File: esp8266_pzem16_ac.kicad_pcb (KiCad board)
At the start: 2 copper layers, 26 x 24 mm, 15 parts, among them J1 RS485, J2 PWR, J3 LED, U1 ESP-12F, U2 AMS1117-3.3

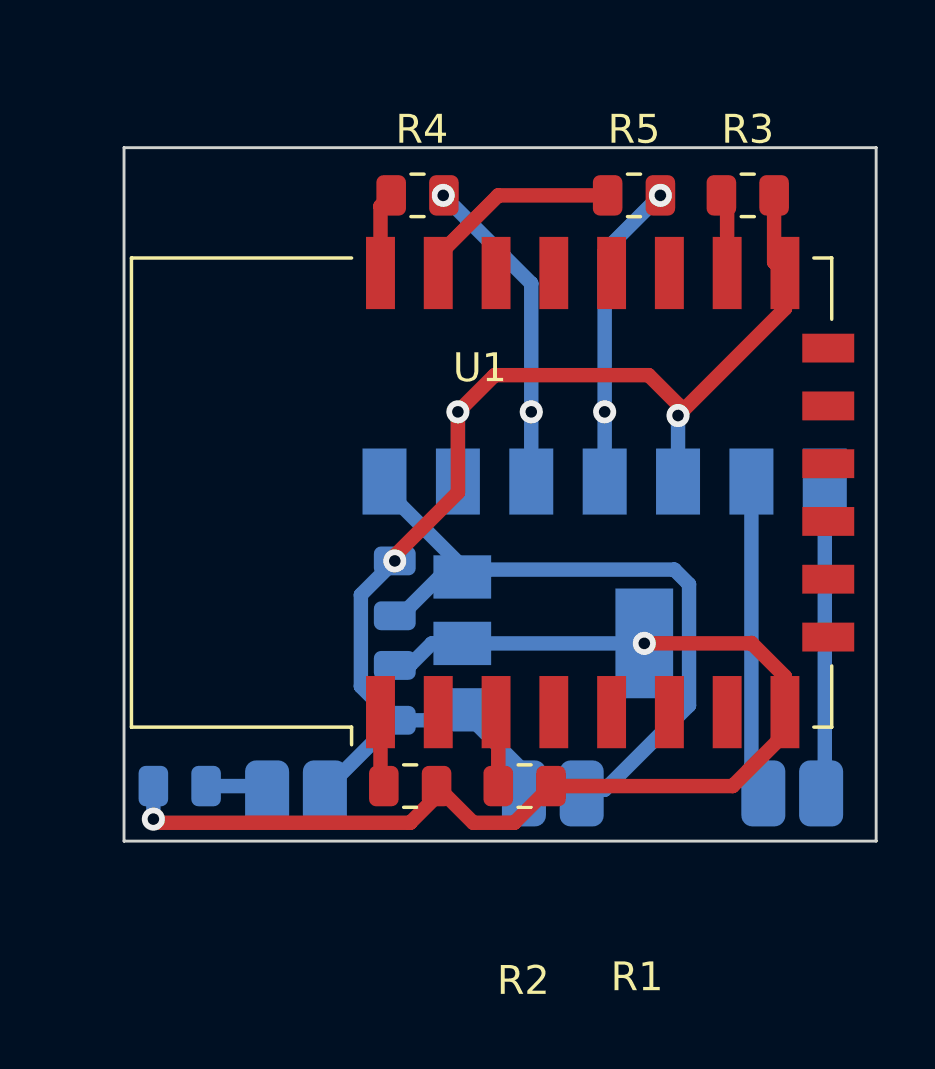
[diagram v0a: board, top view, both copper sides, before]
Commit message: added through hole led pads
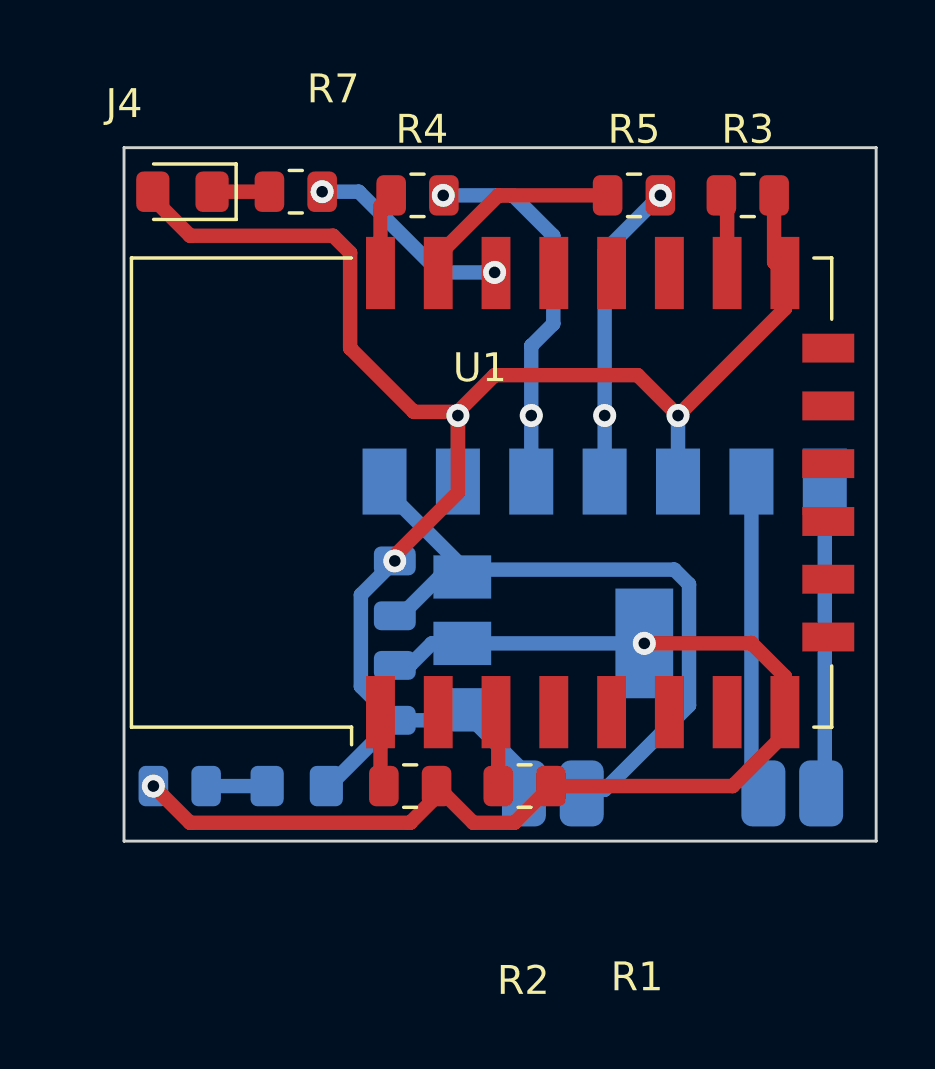
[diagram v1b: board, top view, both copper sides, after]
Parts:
- added J4: LED, LED_SMD:LED_0805_2012Metric_Pad1.15x1.40mm_HandSolder, F.Cu at (62.2, 33.0)
- added R7: 330, Resistor_SMD:R_0805_2012Metric, F.Cu at (66.1, 33.0)
- J3: footprint -local:2pin_pad -> LED_SMD:LED_0805_2012Metric_Pad1.15x1.40mm_HandSolder
- R6: value 0 -> 330
- moved J3 1.06 mm to (66.2, 53.6), turned to 0 degrees
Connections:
- CU1 pad 5: GND -> unconnected-(CU1-Pad5)
- U1 pad 20: unconnected-(U1-Pad20) -> /GPIO_5
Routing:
- net GND: track 44.8 -> 60.3 mm
- net /GPIO_5: track 0.00 -> 7.13 mm, vias 0 -> 2
- net Net-(CU1-Pad3): track 11.2 -> 13.2 mm
- net Net-(J4-Pad1): track 0.00 -> 1.98 mm
- net +3.3V: track 41.9 -> 41.2 mm

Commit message: removed extra files
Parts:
- J3, J4: footprint LED_SMD:LED_0805_2012Metric_Pad1.15x1.40mm_HandSolder -> -local:my_LED_0805_2012Metric_Pad1.15x1.40mm_HandSolder
- moved G*** 1.91 mm to (64.0, 37.0)
- moved R3 0.17 mm to (81.8, 33.0)
- moved R4 0.17 mm to (70.4, 33.0)
- moved R5 0.17 mm to (77.9, 33.0)

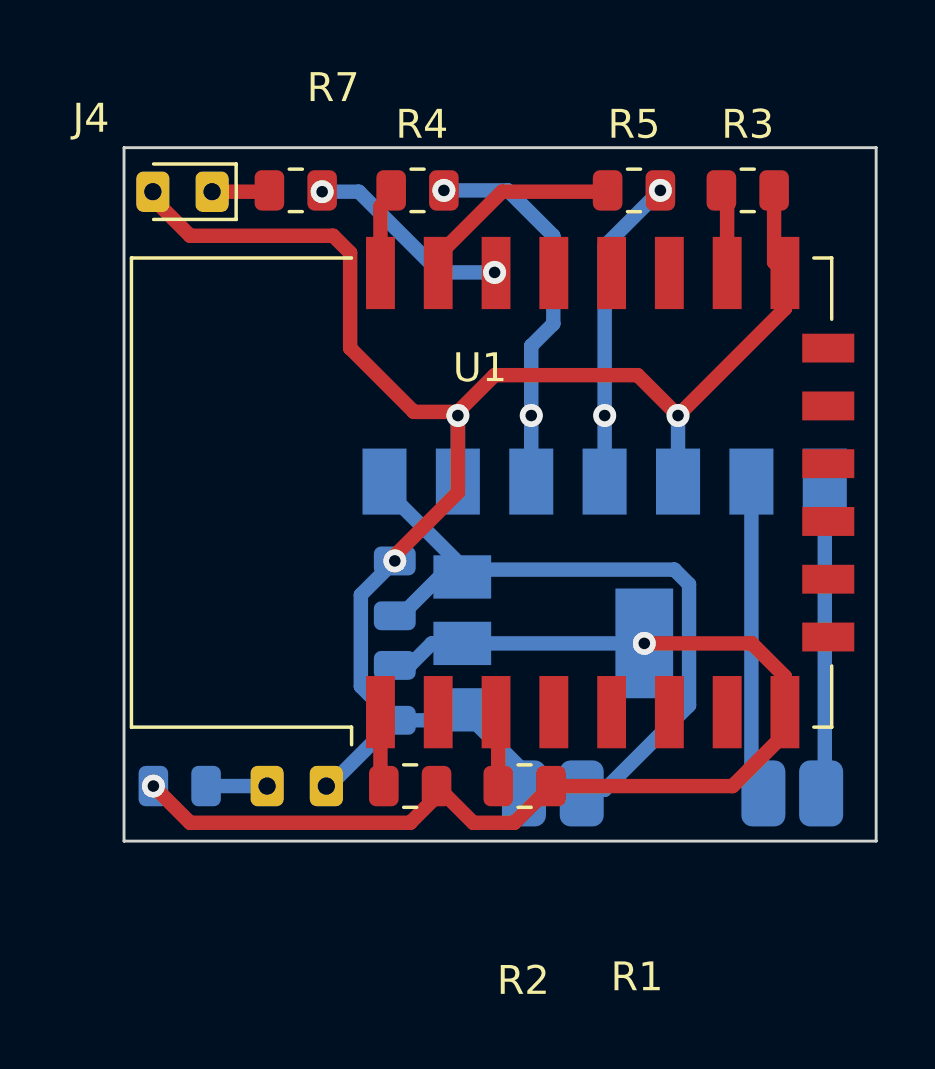
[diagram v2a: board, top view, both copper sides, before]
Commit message: removed more files
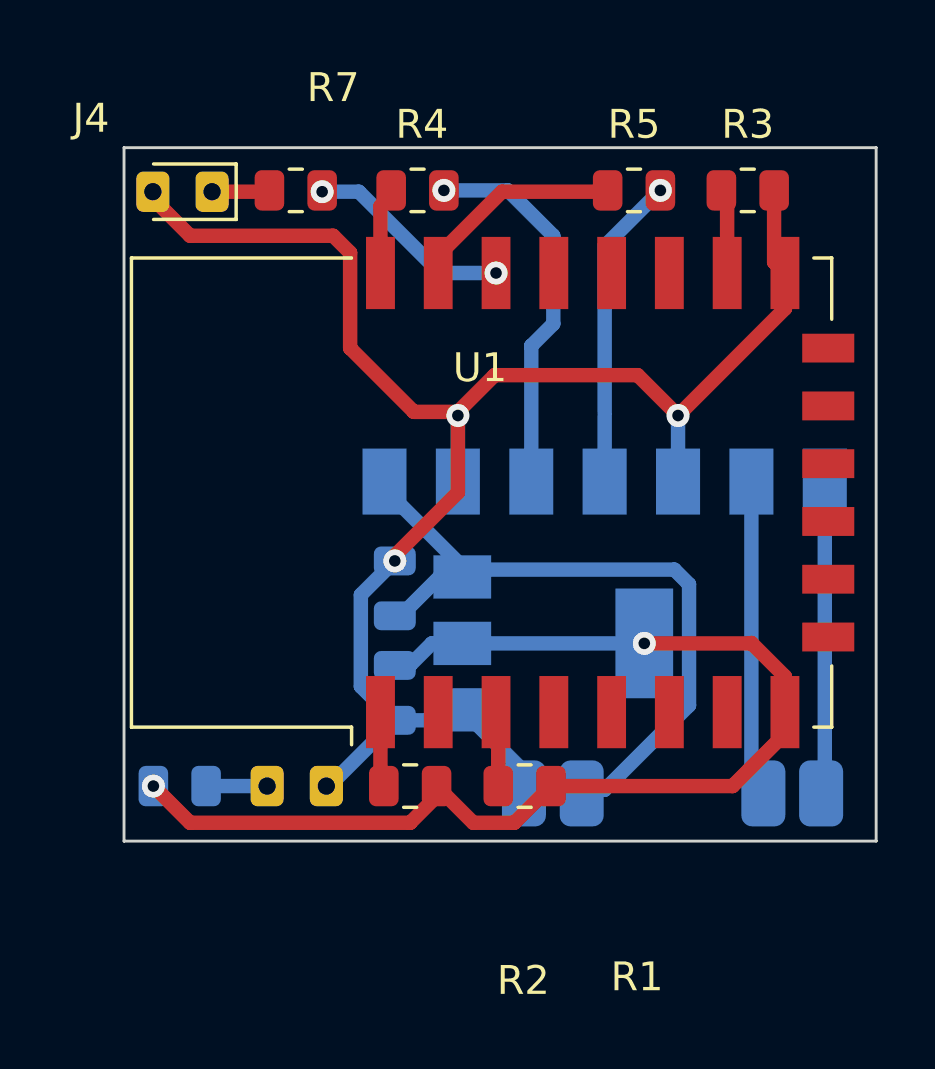
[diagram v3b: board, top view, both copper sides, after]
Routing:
- net Net-(CU1-Pad4): vias 2 -> 1
- net Net-(CU1-Pad3): vias 2 -> 1
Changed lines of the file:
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@@
   (segment (start 69.571 49.417) (end 70.09 49.417) (width 0.5) (layer "B.Cu") (net 3))
   (via (at 71.2705 32.975) (size 0.8) (drill 0.4) (layers "F.Cu" "B.Cu") (net 4))
-  (via (at 74.295 40.767) (size 0.8) (drill 0.4) (layers "F.Cu" "B.Cu") (net 4))
   (segment (start 73.488 32.975) (end 75.057 34.544) (width 0.5) (layer "B.Cu") (net 4))
   (segment (start 74.295 38.354) (end 74.295 43.053) (width 0.5) (layer "B.Cu") (net 4))
@@
   (segment (start 78.74 33.147) (end 78.74 32.9985) (width 0.5) (layer "F.Cu") (net 5))
   (segment (start 78.74 32.9985) (end 78.7635 32.975) (width 0.5) (layer "F.Cu") (net 5))
-  (via (at 76.835 40.767) (size 0.8) (drill 0.4) (layers "F.Cu" "B.Cu") (net 5))
   (via (at 78.7635 32.975) (size 0.8) (drill 0.4) (layers "F.Cu" "B.Cu") (net 5))
   (segment (start 76.835 43.053) (end 76.835 40.767) (width 0.5) (layer "B.Cu") (net 5))
@@
   (segment (start 63.246 33.02) (end 65.231 33.02) (width 0.5) (layer "F.Cu") (net 29))
   (via (at 67.056 33.02) (size 0.8) (drill 0.4) (layers "F.Cu" "B.Cu") (net 30))
-  (via (at 73.025 35.814) (size 0.8) (drill 0.4) (layers "F.Cu" "B.Cu") (net 30))
-  (segment (start 71.12 35.814) (end 73.025 35.814) (width 0.5) (layer "B.Cu") (net 30))
-  (segment (start 67.056 33.02) (end 68.326 33.02) (width 0.5) (layer "B.Cu") (net 30))
-  (segment (start 68.326 33.02) (end 71.12 35.814) (width 0.5) (layer "B.Cu") (net 30))
+  (via (at 73.075 35.834) (size 0.8) (drill 0.4) (layers "F.Cu" "B.Cu") (net 30))
+  (segment (start 73.075 35.834) (end 71.14 35.834) (width 0.5) (layer "B.Cu") (net 30))
+  (segment (start 68.326 33.02) (end 67.056 33.02) (width 0.5) (layer "B.Cu") (net 30))
+  (segment (start 71.14 35.834) (end 68.326 33.02) (width 0.5) (layer "B.Cu") (net 30))
 )
